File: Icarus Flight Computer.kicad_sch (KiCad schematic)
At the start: 4 parts

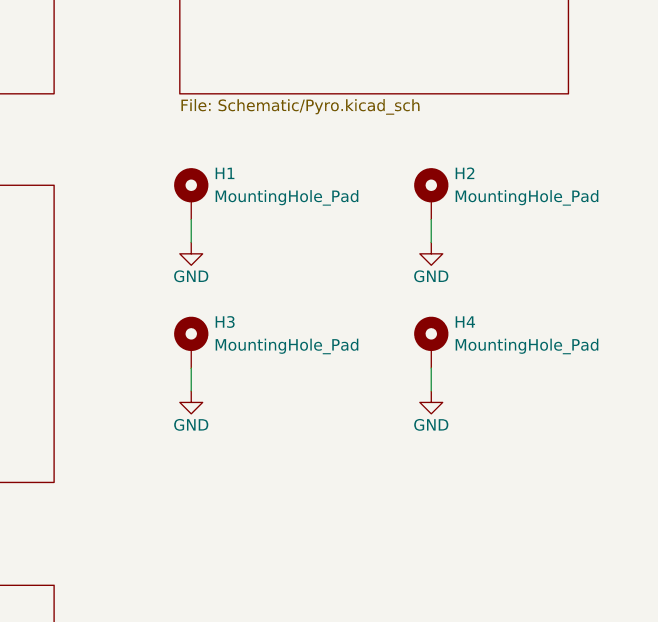
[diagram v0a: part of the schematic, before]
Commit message: Made board smaller
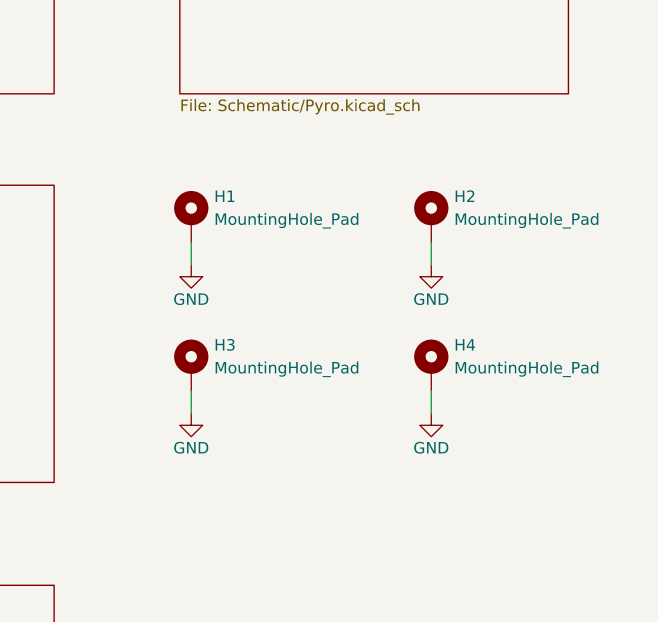
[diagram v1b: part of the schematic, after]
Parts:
- H1, H2, H3, H4: footprint MountingHole:MountingHole_3.2mm_M3_Pad -> MountingHole:MountingHole_2.7mm_M2.5_Pad
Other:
- moved on the sheet: H1, H2, H3, H4

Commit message: V1.0
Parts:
- H1, H2, H3, H4: footprint MountingHole:MountingHole_2.7mm_M2.5_Pad -> MountingHole:MountingHole_2.7mm_M2.5_Pad_Via
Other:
- added sheet Servo (Schematic/Servo.kicad_sch)
- sheet Sensors: file Schematic/Inertial Sensors.kicad_sch -> Schematic/Sensors.kicad_sch
- moved on the sheet: H1, H2, H3, H4
